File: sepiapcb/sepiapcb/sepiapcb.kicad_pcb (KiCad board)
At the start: 2 copper layers, 89.1 x 68.3 mm, 6 parts, among them SW1 SW_DPDT_x2

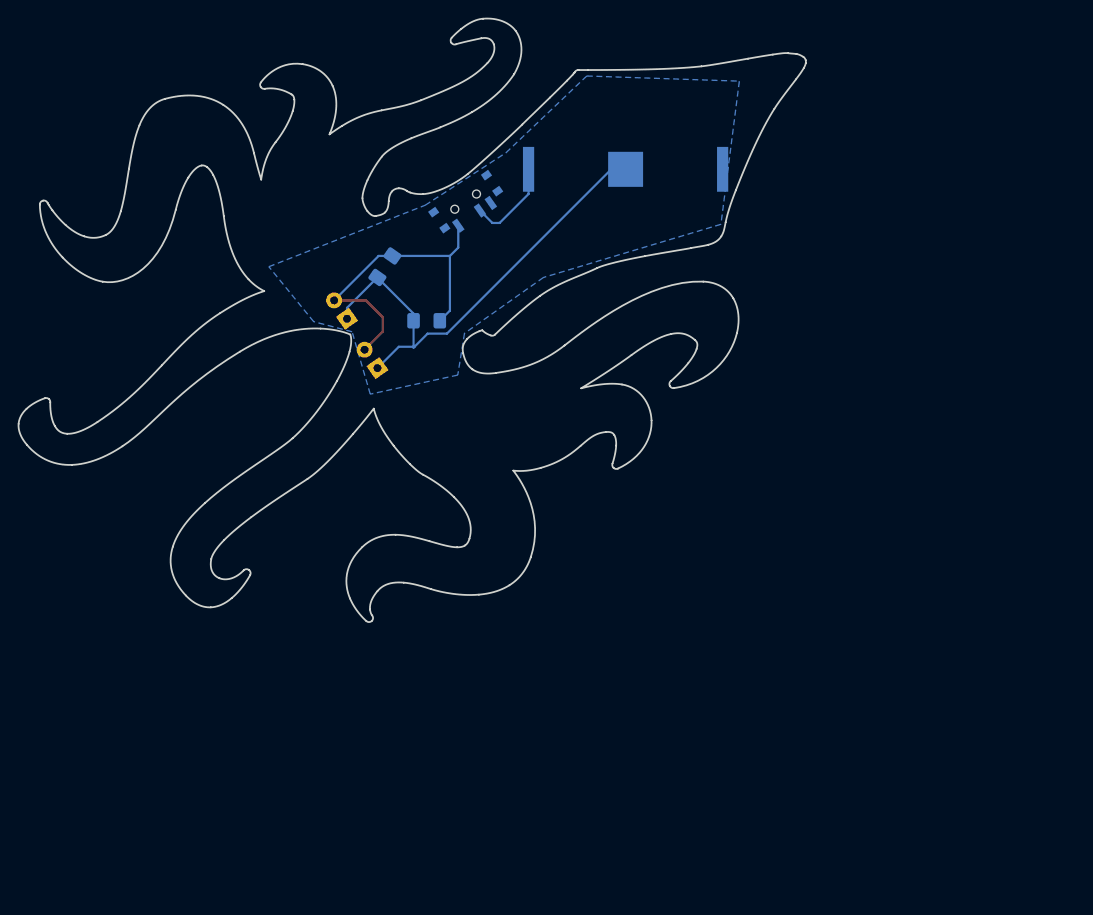
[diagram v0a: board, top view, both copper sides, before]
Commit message: New sepia footprint with pads for THT leds, zone fills for both sides
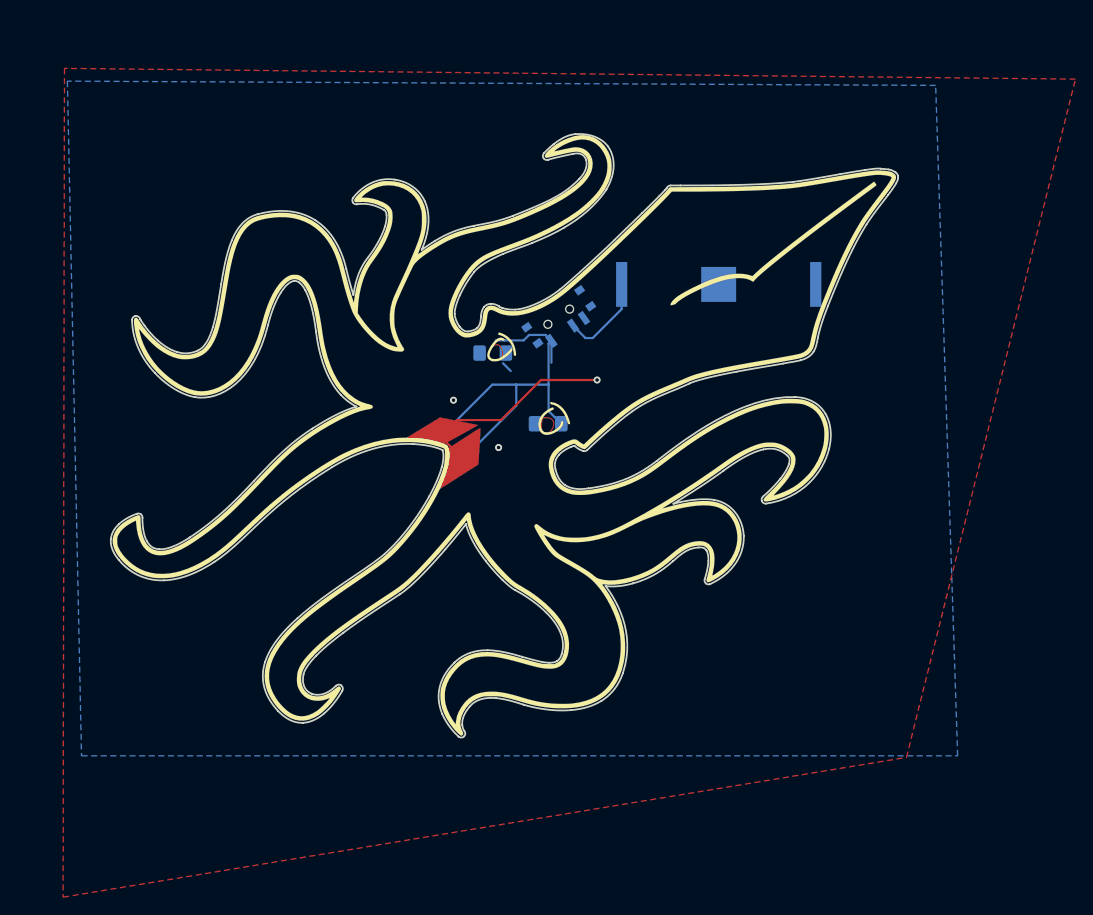
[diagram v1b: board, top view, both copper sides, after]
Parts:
- removed D2: LED, LED_SMD:LED_1206_3216Metric_Pad1.42x1.75mm_HandSolder
- D1: value LED -> LED_Dual_AACC; footprint LED_SMD:LED_1206_3216Metric_Pad1.42x1.75mm_HandSolder -> sepiapcb:sepia_footrprint_pcb; moved to F.Cu
- D3, D4: footprint LED_THT:LED_D5.0mm_Horizontal_O1.27mm_Z3.0mm -> LED_SMD:LED_1206_3216Metric_Pad1.42x1.75mm_HandSolder
- moved D1 26.0 mm to (75.1, 68.7), turned to 0 degrees
- moved D3 20.3 mm to (80.3, 64.1), turned to 0 degrees
- moved D4 17.0 mm to (74.0, 56.1), turned to 180 degrees
- moved BT1 16.8 mm to (99.6, 48.3)
- moved SW1 16.8 mm to (81.7, 52.2)
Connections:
- D1 pad 1: GND -> Net-(D1-Pad1)
- D1 pad 2: Net-(D1-Pad2) -> Net-(D1-Pad1)
- D3 pad 2: Net-(D1-Pad2) -> Net-(D1-Pad1)
- D4 pad 2: Net-(D1-Pad2) -> Net-(D1-Pad1)
- SW1 pad 1: Net-(D1-Pad2) -> Net-(D1-Pad1)
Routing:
- net Net-(D1-Pad1): track 0.00 -> 43.2 mm
- net Net-(D1-Pad2): track 37.6 -> 0.00 mm
- net GND: track 53.3 -> 25.4 mm, vias 0 -> 3
- added copper zone on F.Cu, net GND
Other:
- rule trace_min: 0.2 -> 0.0889

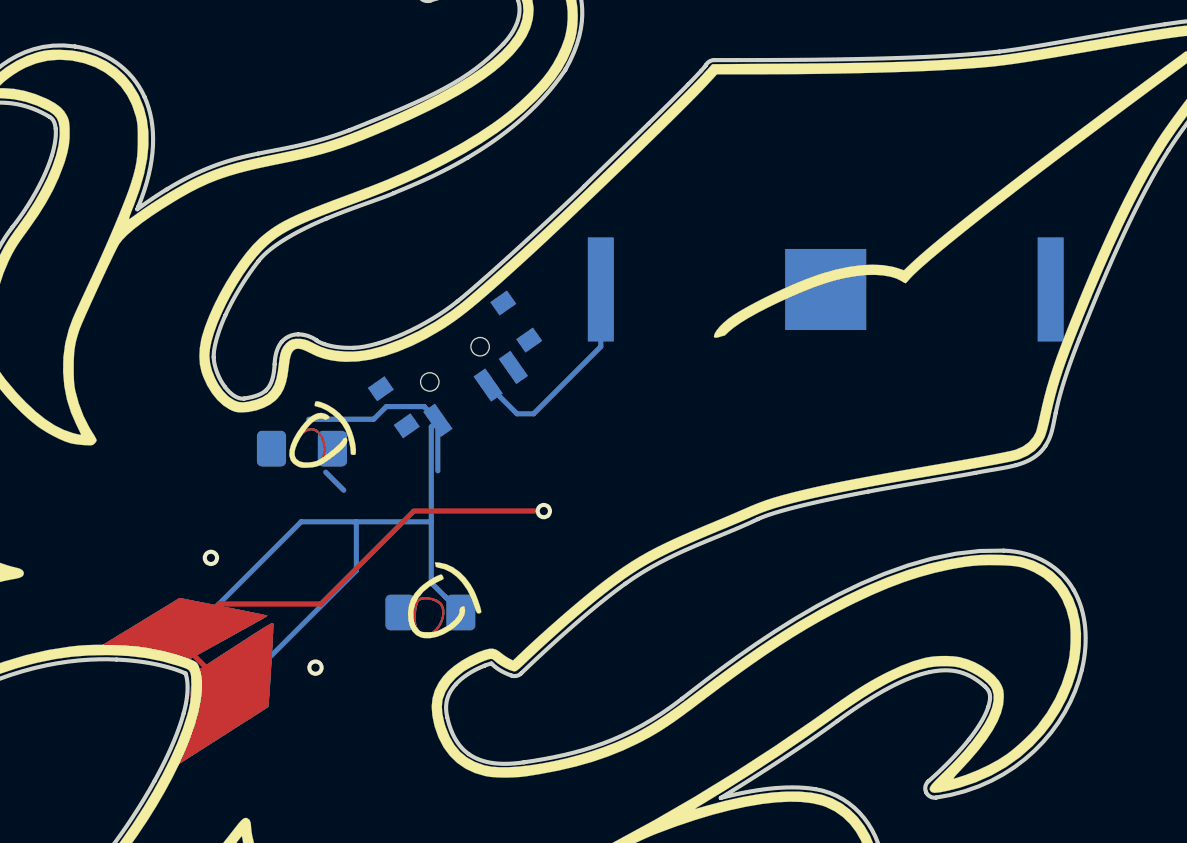
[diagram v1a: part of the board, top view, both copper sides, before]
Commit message: TH coin cell battery holder
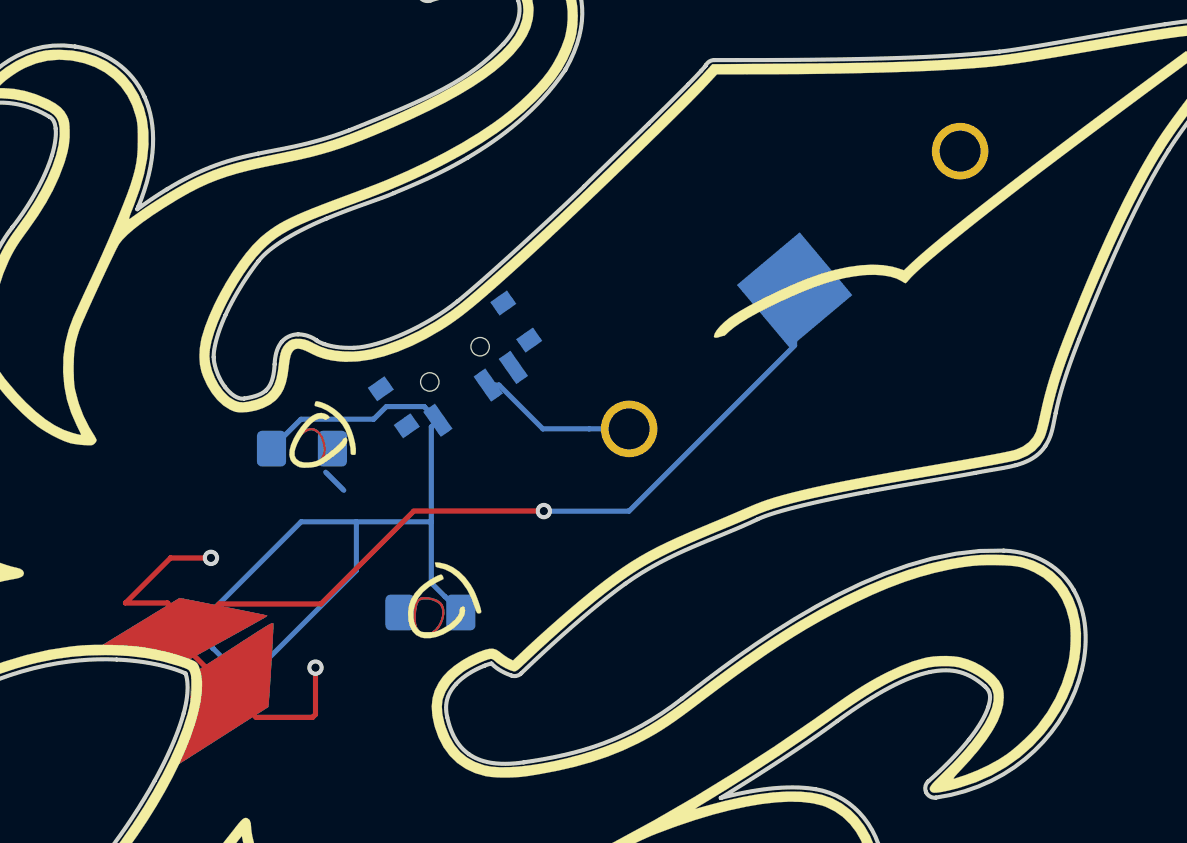
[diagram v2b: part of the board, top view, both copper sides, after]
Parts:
- BT1: footprint Battery:BatteryHolder_Keystone_3034_1x20mm -> Cell_Coin_Holders:Keystone_3003_CR2032_THT
- moved BT1 11.8 mm to (90.0, 55.1), turned to 40 degrees
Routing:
- net GND: track 25.4 -> 60.4 mm
- net Net-(D1-Pad1): track 43.2 -> 46.8 mm
- net +3V0: track 10.2 -> 7.77 mm
